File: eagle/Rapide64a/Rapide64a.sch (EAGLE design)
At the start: 28 parts, among them IC1 MEGA64-A, J1 AVR_SPI_PRG_6PTH

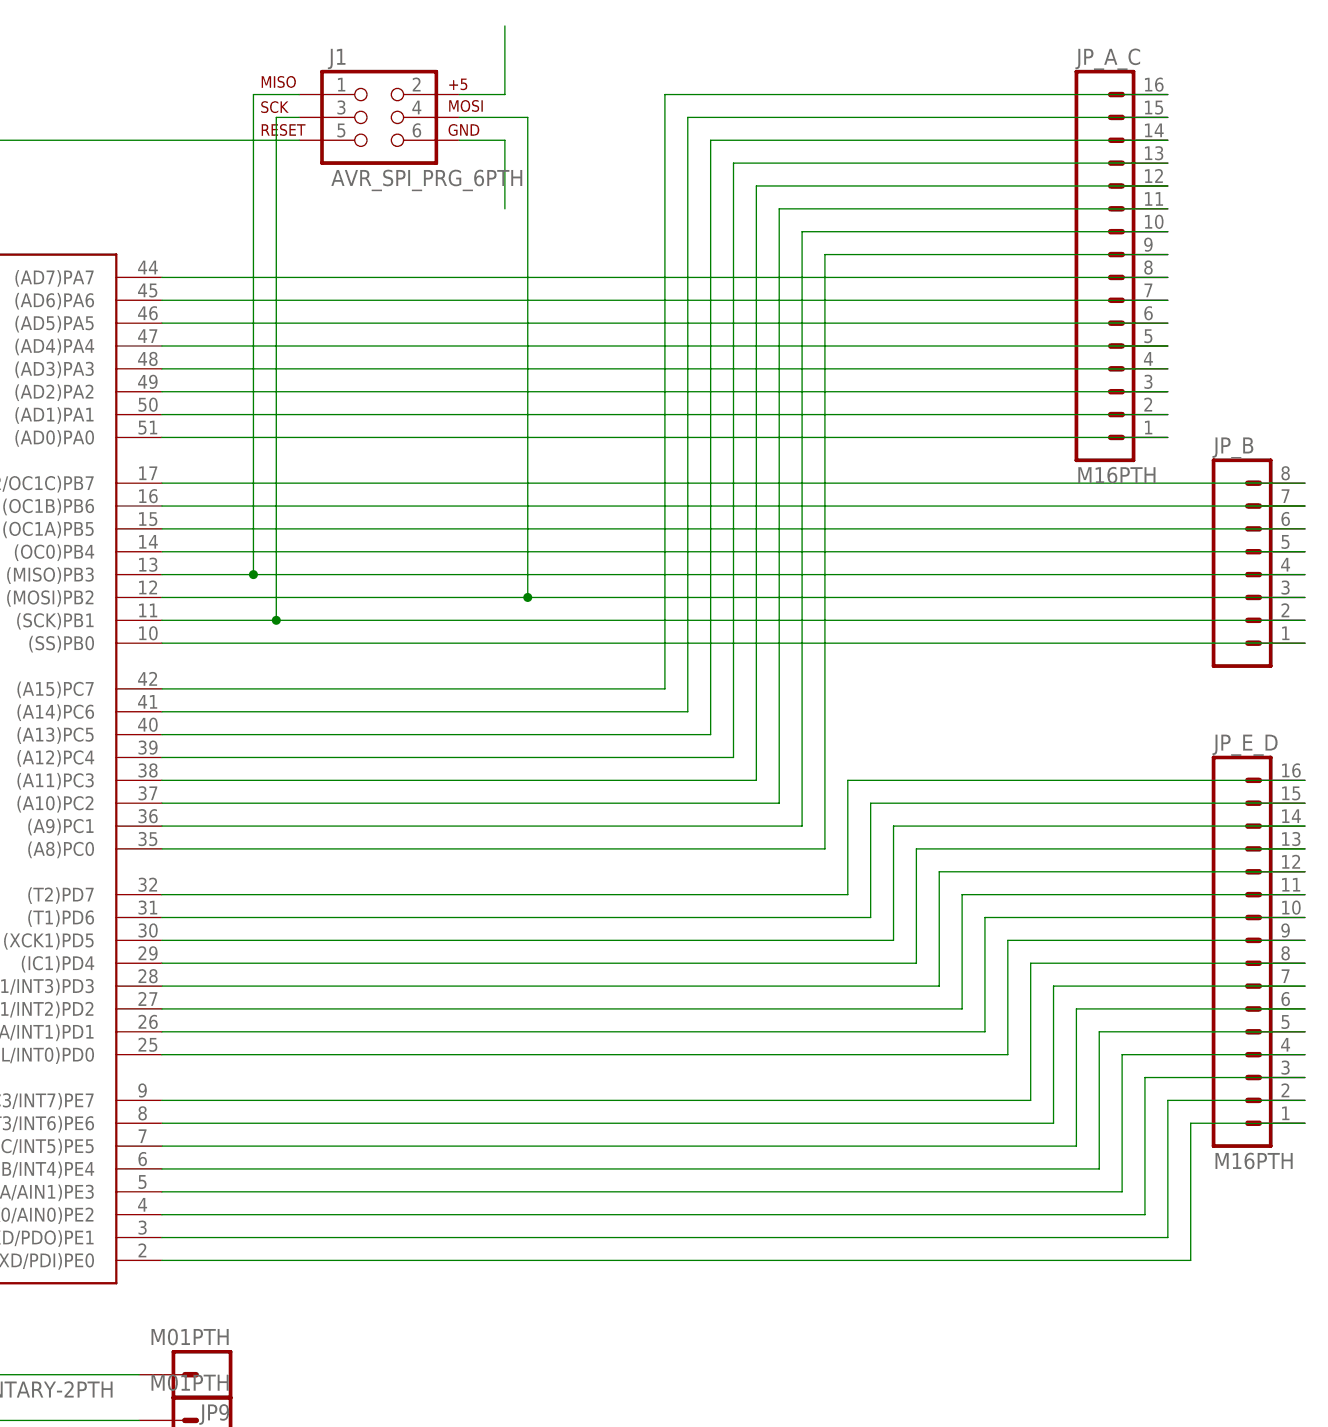
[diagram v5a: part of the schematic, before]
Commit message: v1.1 in progress : rewired with correct pins PE0 and PE1 for programming
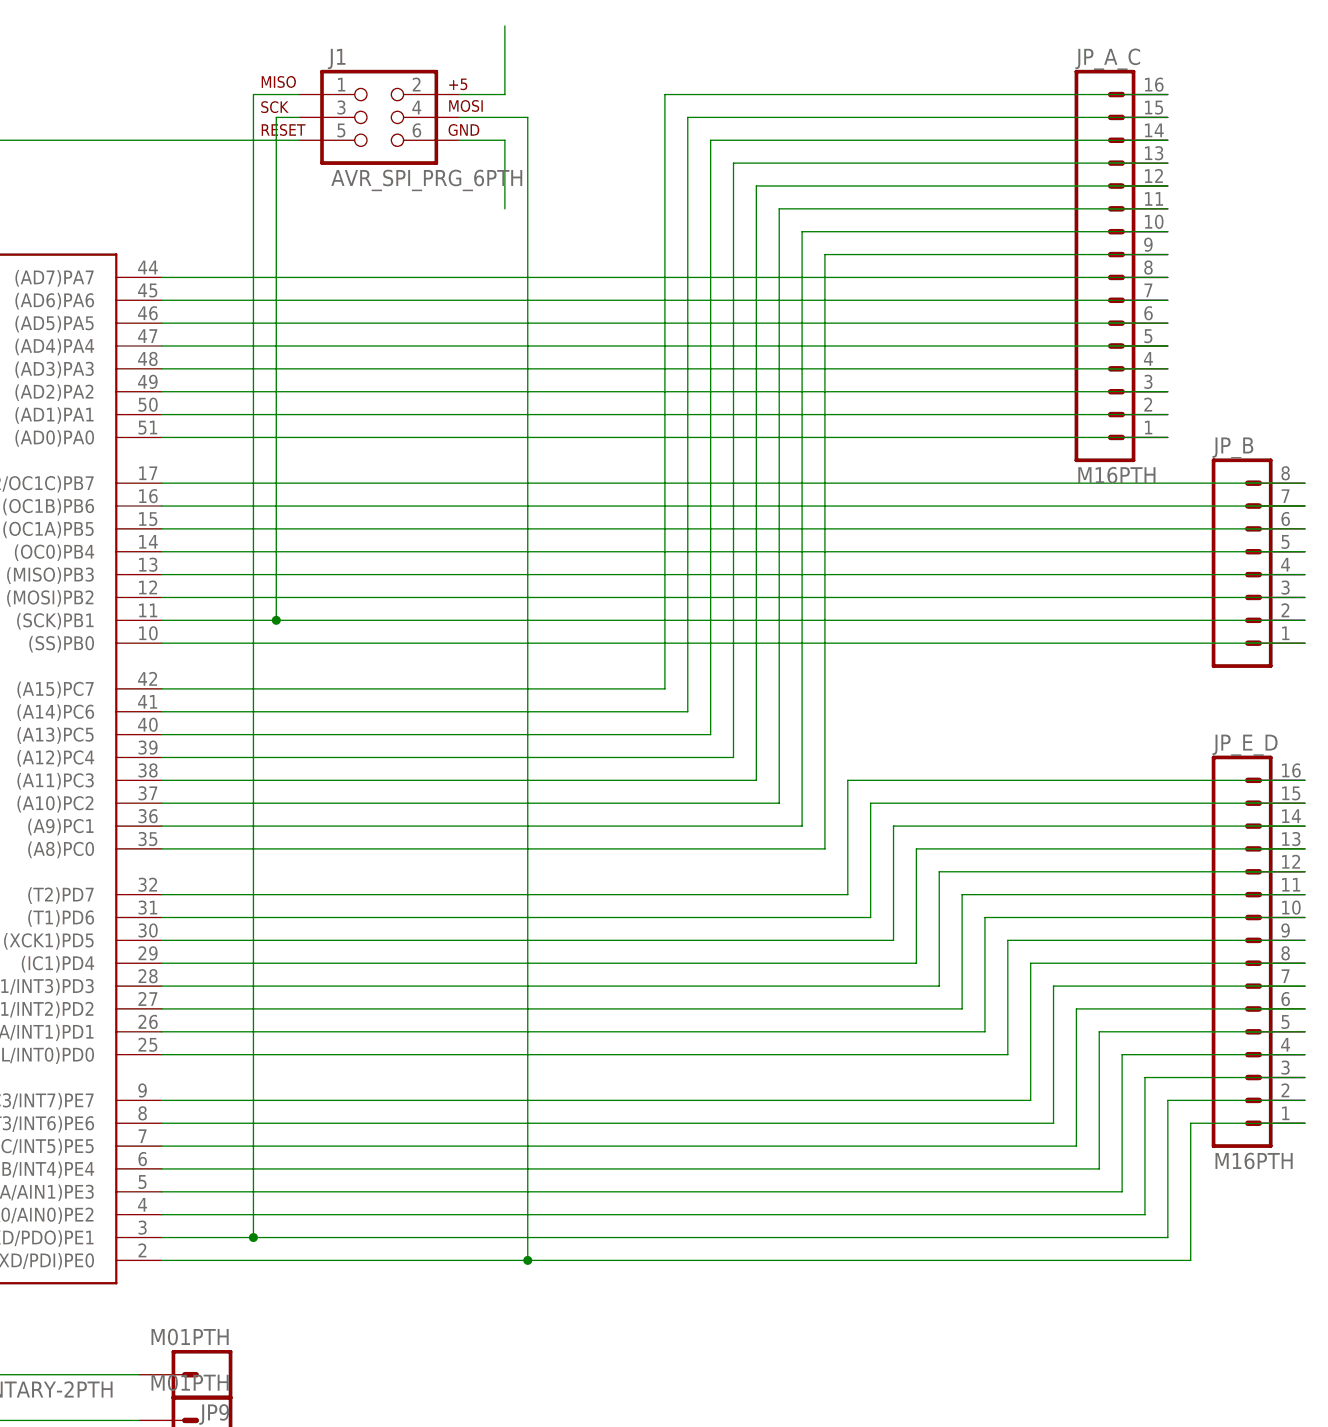
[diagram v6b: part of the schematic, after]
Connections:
- net N$15 renamed SCK
- net N$57 renamed RESET
- removed net N$1: IC1.(RXD/PDI)PE0, JP_E_D.1
- removed net N$61: IC1.(TXD/PDO)PE1, JP_E_D.2
- new net MISO: IC1.(TXD/PDO)PE1, J1.1, JP_E_D.2
- new net MOSI: IC1.(RXD/PDI)PE0, J1.4, JP_E_D.1
- net N$35: no longer J1.4
- net N$36: no longer J1.1
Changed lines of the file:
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@@
 </busses>
 <nets>
-<net name="N$1" class="0">
-<segment>
-<pinref part="IC1" gate="G$1" pin="(RXD/PDI)PE0"/>
-<wire x1="73.66" y1="7.62" x2="187.96" y2="7.62" width="0.1524" layer="91"/>
-<wire x1="187.96" y1="7.62" x2="187.96" y2="22.86" width="0.1524" layer="91"/>
-<pinref part="JP_E_D" gate="G$1" pin="1"/>
-<wire x1="187.96" y1="22.86" x2="200.66" y2="22.86" width="0.1524" layer="91"/>
-</segment>
-</net>
-<net name="N$61" class="0">
-<segment>
-<pinref part="IC1" gate="G$1" pin="(TXD/PDO)PE1"/>
-<wire x1="73.66" y1="10.16" x2="185.42" y2="10.16" width="0.1524" layer="91"/>
-<wire x1="185.42" y1="10.16" x2="185.42" y2="25.4" width="0.1524" layer="91"/>
-<pinref part="JP_E_D" gate="G$1" pin="2"/>
-<wire x1="185.42" y1="25.4" x2="200.66" y2="25.4" width="0.1524" layer="91"/>
-</segment>
-</net>
 <net name="N$62" class="0">
 <segment>
@@
 </segment>
 </net>
-<net name="N$15" class="0">
+<net name="SCK" class="0">
 <segment>
 <pinref part="IC1" gate="G$1" pin="(SCK)PB1"/>
@@
 <pinref part="IC1" gate="G$1" pin="(MOSI)PB2"/>
 <pinref part="JP_B" gate="G$1" pin="3"/>
-<wire x1="73.66" y1="81.28" x2="114.3" y2="81.28" width="0.1524" layer="91"/>
-<pinref part="J1" gate="G$1" pin="4"/>
-<wire x1="114.3" y1="81.28" x2="200.66" y2="81.28" width="0.1524" layer="91"/>
-<wire x1="106.68" y1="134.62" x2="114.3" y2="134.62" width="0.1524" layer="91"/>
-<wire x1="114.3" y1="134.62" x2="114.3" y2="81.28" width="0.1524" layer="91"/>
-<junction x="114.3" y="81.28"/>
+<wire x1="73.66" y1="81.28" x2="200.66" y2="81.28" width="0.1524" layer="91"/>
 </segment>
 </net>
@@
 <pinref part="IC1" gate="G$1" pin="(MISO)PB3"/>
 <pinref part="JP_B" gate="G$1" pin="4"/>
-<wire x1="73.66" y1="83.82" x2="83.82" y2="83.82" width="0.1524" layer="91"/>
-<pinref part="J1" gate="G$1" pin="1"/>
-<wire x1="83.82" y1="83.82" x2="200.66" y2="83.82" width="0.1524" layer="91"/>
-<wire x1="88.9" y1="137.16" x2="83.82" y2="137.16" width="0.1524" layer="91"/>
-<wire x1="83.82" y1="137.16" x2="83.82" y2="83.82" width="0.1524" layer="91"/>
-<junction x="83.82" y="83.82"/>
+<wire x1="73.66" y1="83.82" x2="200.66" y2="83.82" width="0.1524" layer="91"/>
 </segment>
 </net>
@@
 </segment>
 </net>
-<net name="N$57" class="0">
+<net name="RESET" class="0">
 <segment>
 <pinref part="JP_X" gate="G$1" pin="2"/>
@@
 </segment>
 </net>
+<net name="MOSI" class="0">
+<segment>
+<pinref part="J1" gate="G$1" pin="4"/>
+<wire x1="106.68" y1="134.62" x2="114.3" y2="134.62" width="0.1524" layer="91"/>
+<pinref part="IC1" gate="G$1" pin="(RXD/PDI)PE0"/>
+<wire x1="73.66" y1="7.62" x2="114.3" y2="7.62" width="0.1524" layer="91"/>
+<wire x1="114.3" y1="7.62" x2="187.96" y2="7.62" width="0.1524" layer="91"/>
+<wire x1="187.96" y1="7.62" x2="187.96" y2="22.86" width="0.1524" layer="91"/>
+<pinref part="JP_E_D" gate="G$1" pin="1"/>
+<wire x1="187.96" y1="22.86" x2="200.66" y2="22.86" width="0.1524" layer="91"/>
+<wire x1="114.3" y1="134.62" x2="114.3" y2="7.62" width="0.1524" layer="91"/>
+<junction x="114.3" y="7.62"/>
+</segment>
+</net>
+<net name="MISO" class="0">
+<segment>
+<pinref part="J1" gate="G$1" pin="1"/>
+<wire x1="88.9" y1="137.16" x2="83.82" y2="137.16" width="0.1524" layer="91"/>
+<pinref part="IC1" gate="G$1" pin="(TXD/PDO)PE1"/>
+<wire x1="73.66" y1="10.16" x2="83.82" y2="10.16" width="0.1524" layer="91"/>
+<wire x1="83.82" y1="10.16" x2="185.42" y2="10.16" width="0.1524" layer="91"/>
+<wire x1="185.42" y1="10.16" x2="185.42" y2="25.4" width="0.1524" layer="91"/>
+<pinref part="JP_E_D" gate="G$1" pin="2"/>
+<wire x1="185.42" y1="25.4" x2="200.66" y2="25.4" width="0.1524" layer="91"/>
+<wire x1="83.82" y1="137.16" x2="83.82" y2="10.16" width="0.1524" layer="91"/>
+<junction x="83.82" y="10.16"/>
+</segment>
+</net>
